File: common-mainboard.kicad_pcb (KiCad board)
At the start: 2 copper layers, 77.5 x 49.5 mm, 92 parts, among them J1 SIM_Card, J2 RSP-122811-01, J3 Conn_01x02_Female, J4 S4B-ZR-SM4A-TF(LF)(SN), Q1 DTC043ZEB, Q2 DTC043ZEB, Q3 DTC043ZEB, SW1 SW_Push, SW2 SW_Push, U1 ATSAMD21J18A-M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

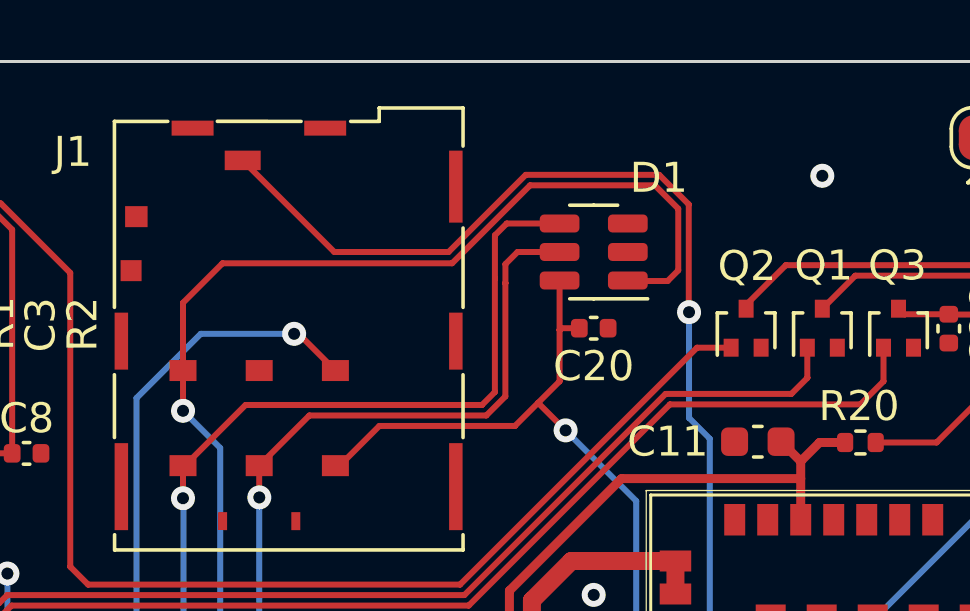
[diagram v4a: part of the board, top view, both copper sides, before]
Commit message: sim card: added RF filtering passive components
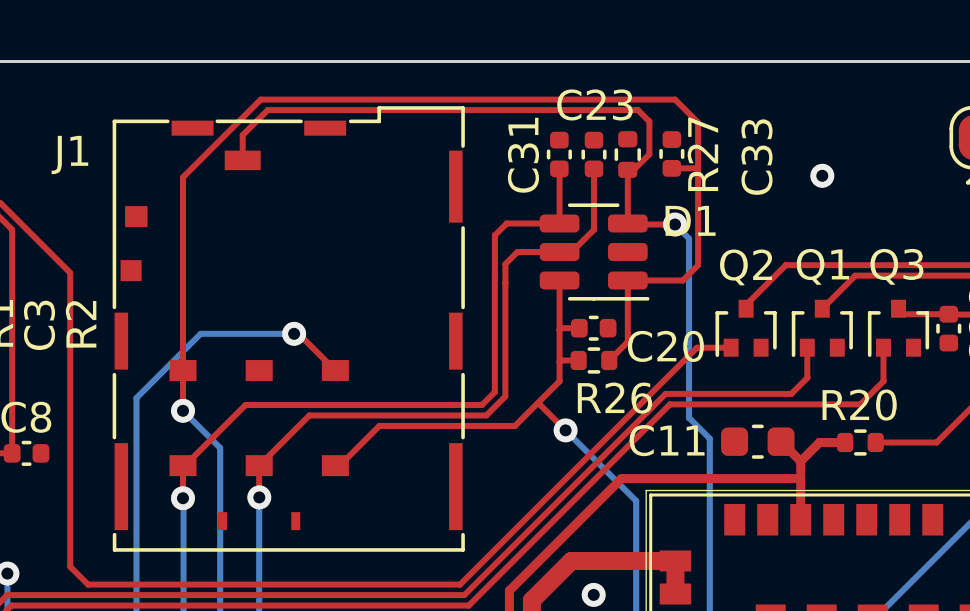
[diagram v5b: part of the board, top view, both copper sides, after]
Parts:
- added C23: 33pF, Capacitor_SMD:C_0402_1005Metric, F.Cu at (114.3, 104.7)
- added C31: 33pF, Capacitor_SMD:C_0402_1005Metric, F.Cu at (113.2, 104.7)
- added C33: 33pF, Capacitor_SMD:C_0402_1005Metric, F.Cu at (116.9, 104.7)
- added R26: 15k, Resistor_SMD:R_0402_1005Metric, F.Cu at (114.3, 111.6)
- added R27: 51k, Resistor_SMD:R_0402_1005Metric, F.Cu at (115.4, 104.7)
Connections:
- D1 pad 3: unconnected-(D1-Pad3) -> USIM1_DET
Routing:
- net USIM1_DATA: track 58.7 -> 70.2 mm
- net USIM1_RST: track 44.7 -> 48.2 mm
- net USIM1_DET: track 42.5 -> 44.7 mm
- net USIM1_CLK: track 50.7 -> 52.5 mm
- net USIM1_VDD: track 33.3 -> 34.0 mm

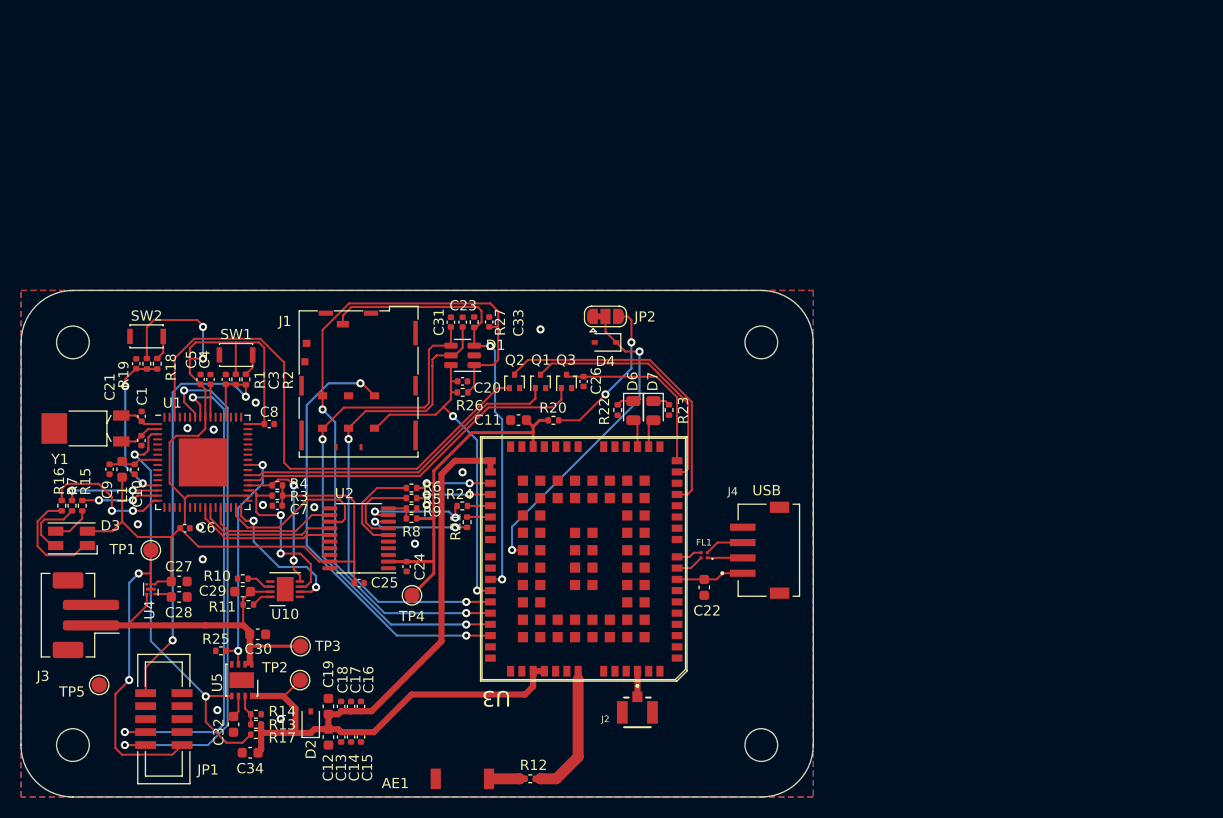
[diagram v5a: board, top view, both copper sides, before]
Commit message: added connectors for I2C and SPI extensions
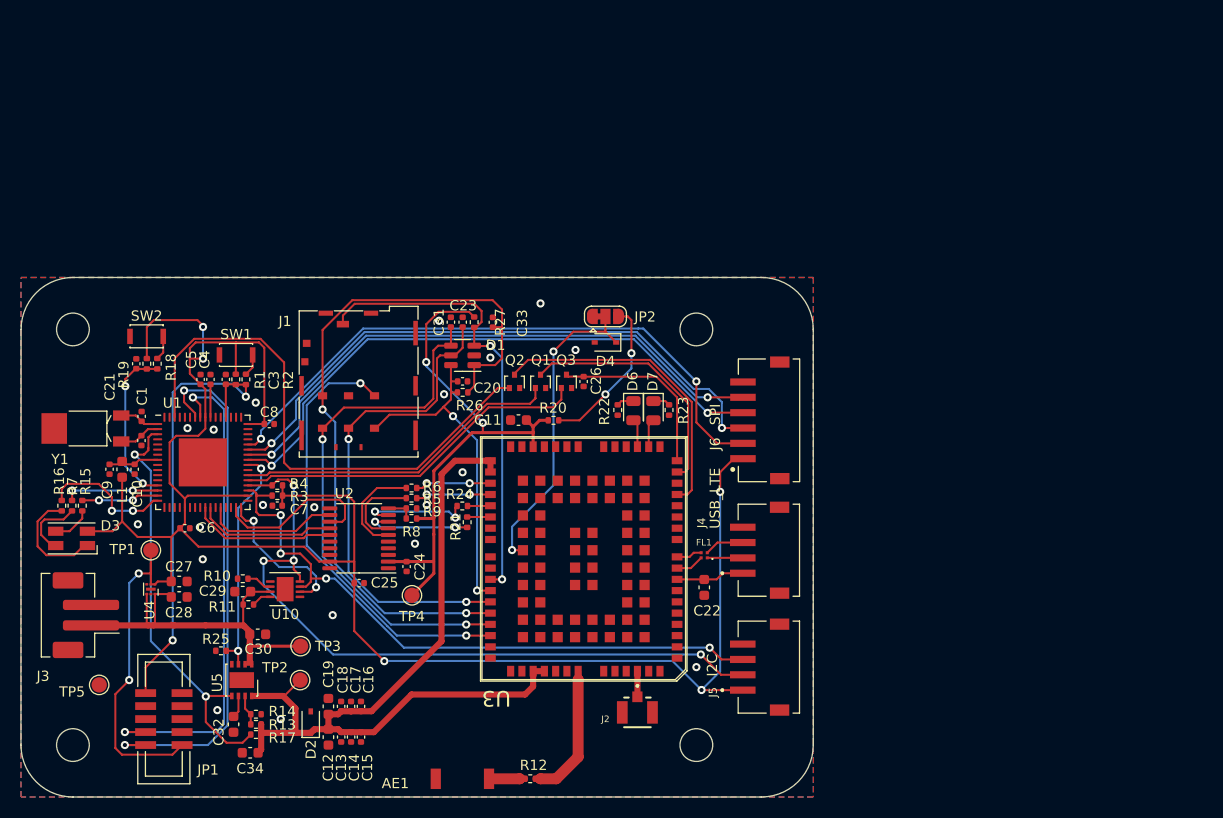
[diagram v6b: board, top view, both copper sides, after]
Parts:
- added J5: S4B-ZR-SM4A-TF(LF)(SN), S4B-ZR-SM4A-TF_LF__SN_:JST_S4B-ZR-SM4A-TF(LF)(SN), F.Cu at (141.7, 138.4)
- added J6: S6B-ZR-SM4A-TF(LF)(SN), S6B-ZR-SM4A-TF_LF__SN_:JST_S6B-ZR-SM4A-TF(LF)(SN), F.Cu at (141.7, 114.3)
- moved H3 6.48 mm to (137.2, 105.4)
- moved H2 6.35 mm to (137.2, 146.1)
- moved H4 1.27 mm to (76.2, 105.4)
- moved C33 0.36 mm to (117.3, 104.7)
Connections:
- U1 pad 41: unconnected-(U1-Pad41) -> MISO
- U1 pad 42: unconnected-(U1-Pad42) -> /CS
- U1 pad 43: unconnected-(U1-Pad43) -> MOSI
- U1 pad 44: unconnected-(U1-Pad44) -> SCK
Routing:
- net +3V3: track 150.0 -> 219.9 mm, vias 4 -> 7
- net SCK: track 0.00 -> 60.6 mm, vias 0 -> 2
- net MOSI: track 0.00 -> 59.6 mm, vias 0 -> 2
- net MISO: track 0.00 -> 58.5 mm, vias 0 -> 2
- net /CS: track 0.00 -> 57.1 mm, vias 0 -> 2
- net SCL: track 14.6 -> 70.4 mm, vias 2 -> 4
- net SDA: track 17.0 -> 62.5 mm, vias 2 -> 4
- net VDD_EXT: track 35.2 -> 53.5 mm, vias 0 -> 2
- net USIM1_DATA: track 70.2 -> 71.3 mm
- net VBAT: track 39.4 -> 38.7 mm
- net GNDREF: vias 14 -> 20
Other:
- board size 77.5 x 49.5 mm -> 77.5 x 50.8 mm
- board text added: "I2C"
- board text added: "SPI"
- board text added: "USB_LTE"
- board text removed: "USB"

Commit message: updated footprints and PCB
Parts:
- C32: footprint Capacitor_SMD:C_0603_1608Metric -> Capacitor_SMD:C_0201_0603Metric
- C34: value 1uF -> 10uF
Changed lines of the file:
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@@
     )
   )
-  (footprint "Capacitor_SMD:C_0603_1608Metric" (layer "F.Cu")
+  (footprint "Capacitor_SMD:C_0201_0603Metric" (layer "F.Cu")
     (at 91.904857 144.026066 -90)
-    (descr "Capacitor SMD 0603 (1608 Metric), square (rectangular) end terminal, IPC_7351 nominal, (Body size source: IPC-SM-782 page 76, https://www.pcb-3d.com/wordpress/wp-content/uploads/ipc-sm-782a_amendment_1_and_2.pdf), generated with kicad-footprint-generator")
+    (descr "Capacitor SMD 0201 (0603 Metric), square (rectangular) end terminal, IPC_7351 nominal, (Body size source: https://www.vishay.com/docs/20052/crcw0201e3.pdf), generated with kicad-footprint-generator")
     (tags "capacitor")
     (property "Sheetfile" "lipo-power-supply.kicad_sch")
     (property "Sheetname" "lipo-power-supply")
     (attr smd)
-    (fp_text reference "C32" (at 0.753934 1.443504 90) (layer "F.SilkS")
+    (fp_text reference "C32" (at 0 -1.05 -90) (layer "F.SilkS")
       (effects (font (size 1 1) (thickness 0.15)))
     )
-    (fp_text value "1000pF" (at 0 1.43 90) (layer "F.Fab")
+    (fp_text value "1000pF" (at 0 1.05 -90) (layer "F.Fab")
       (effects (font (size 1 1) (thickness 0.15)))
     )
-    (fp_text user "${REFERENCE}" (at 0 0 90) (layer "F.Fab")
-      (effects (font (size 0.4 0.4) (thickness 0.06)))
+    (fp_text user "${REFERENCE}" (at 0 -0.68 -90) (layer "F.Fab")
+      (effects (font (size 0.25 0.25) (thickness 0.04)))
     )
-    (fp_line (start -0.14058 -0.51) (end 0.14058 -0.51) (layer "F.SilkS") (width 0.12))
-    (fp_line (start -0.14058 0.51) (end 0.14058 0.51) (layer "F.SilkS") (width 0.12))
-    (fp_line (start 1.48 0.73) (end -1.48 0.73) (layer "F.CrtYd") (width 0.05))
-    (fp_line (start 1.48 -0.73) (end 1.48 0.73) (layer "F.CrtYd") (width 0.05))
-    (fp_line (start -1.48 0.73) (end -1.48 -0.73) (layer "F.CrtYd") (width 0.05))
-    (fp_line (start -1.48 -0.73) (end 1.48 -0.73) (layer "F.CrtYd") (width 0.05))
-    (fp_line (start -0.8 -0.4) (end 0.8 -0.4) (layer "F.Fab") (width 0.1))
-    (fp_line (start -0.8 0.4) (end -0.8 -0.4) (layer "F.Fab") (width 0.1))
-    (fp_line (start 0.8 0.4) (end -0.8 0.4) (layer "F.Fab") (width 0.1))
-    (fp_line (start 0.8 -0.4) (end 0.8 0.4) (layer "F.Fab") (width 0.1))
-    (pad "1" smd roundrect (at -0.775 0 270) (size 0.9 0.95) (layers "F.Cu" "F.Paste" "F.Mask") (roundrect_rratio 0.25)
+    (fp_line (start 0.7 0.35) (end -0.7 0.35) (layer "F.CrtYd") (width 0.05))
+    (fp_line (start 0.7 -0.35) (end 0.7 0.35) (layer "F.CrtYd") (width 0.05))
+    (fp_line (start -0.7 0.35) (end -0.7 -0.35) (layer "F.CrtYd") (width 0.05))
+    (fp_line (start -0.7 -0.35) (end 0.7 -0.35) (layer "F.CrtYd") (width 0.05))
+    (fp_line (start -0.3 -0.15) (end 0.3 -0.15) (layer "F.Fab") (width 0.1))
+    (fp_line (start -0.3 0.15) (end -0.3 -0.15) (layer "F.Fab") (width 0.1))
+    (fp_line (start 0.3 0.15) (end -0.3 0.15) (layer "F.Fab") (width 0.1))
+    (fp_line (start 0.3 -0.15) (end 0.3 0.15) (layer "F.Fab") (width 0.1))
+    (pad "" smd roundrect (at 0.345 0 270) (size 0.318 0.36) (layers "F.Paste") (roundrect_rratio 0.25))
+    (pad "" smd roundrect (at -0.345 0 270) (size 0.318 0.36) (layers "F.Paste") (roundrect_rratio 0.25))
+    (pad "1" smd roundrect (at -0.32 0 270) (size 0.46 0.4) (layers "F.Cu" "F.Mask") (roundrect_rratio 0.25)
       (net 53 "Net-(C32-Pad1)") (pintype "passive"))
-    (pad "2" smd roundrect (at 0.775 0 270) (size 0.9 0.95) (layers "F.Cu" "F.Paste" "F.Mask") (roundrect_rratio 0.25)
+    (pad "2" smd roundrect (at 0.32 0 270) (size 0.46 0.4) (layers "F.Cu" "F.Mask") (roundrect_rratio 0.25)
       (net 2 "GNDREF") (pintype "passive"))
-    (model "${KICAD6_3DMODEL_DIR}/Capacitor_SMD.3dshapes/C_0603_1608Metric.wrl"
+    (model "${KICAD6_3DMODEL_DIR}/Capacitor_SMD.3dshapes/C_0201_0603Metric.wrl"
       (offset (xyz 0 0 0))
       (scale (xyz 1 1 1))
@@
       (effects (font (size 1 1) (thickness 0.15)))
     )
-    (fp_text value "1uF" (at 0 1.43) (layer "F.Fab")
+    (fp_text value "10uF" (at 0 1.43) (layer "F.Fab")
       (effects (font (size 1 1) (thickness 0.15)))
     )
@@
   (segment (start 92.385 141.25) (end 92.385 142.770923) (width 0.2) (layer "F.Cu") (net 53))
   (segment (start 92.385 142.770923) (end 91.904857 143.251066) (width 0.2) (layer "F.Cu") (net 53))
+  (segment (start 91.904857 143.251066) (end 91.904857 143.706066) (width 0.2) (layer "F.Cu") (net 53))
   (segment (start 84.4875 115.16) (end 83.538085 115.16) (width 0.2) (layer "F.Cu") (net 54))
   (segment (start 80.923405 116.366368) (end 82.331717 116.366368) (width 0.2) (layer "F.Cu") (net 54))

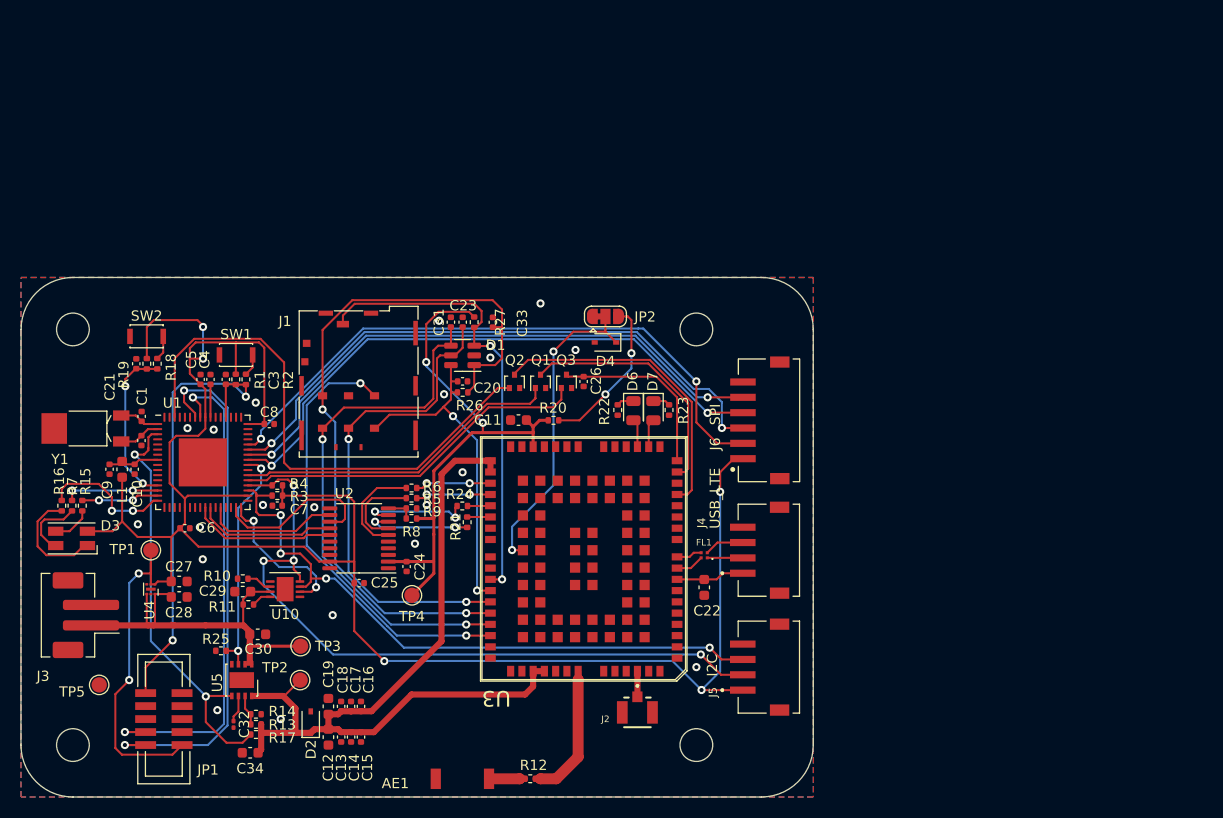
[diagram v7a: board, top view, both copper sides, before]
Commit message: fixed SIM card orientation
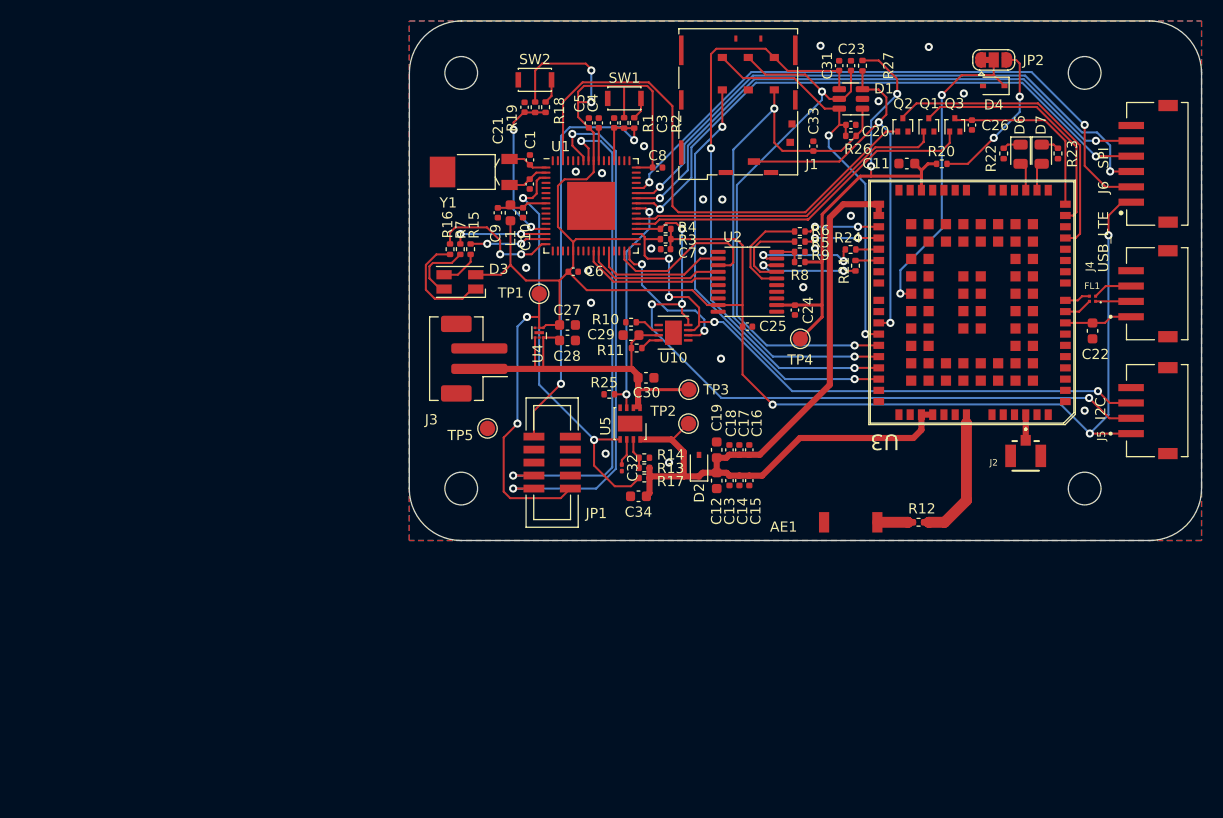
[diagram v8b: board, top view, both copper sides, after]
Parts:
- added G***: LOGO, LOGO, B.Cu at (147.2, 100.7)
- moved J1 50.1 mm to (142.2, 81.3), turned to 0 degrees
- moved R23 45.6 mm to (172.5, 88.2)
- moved AE1 45.5 mm to (151.9, 129.3)
- moved C12 45.5 mm to (139.1, 120.2)
- moved C13 45.5 mm to (140.4, 120.2)
- moved C20 45.5 mm to (152.3, 85.4)
- moved C23 45.5 mm to (152.3, 79.6)
- moved C3 45.5 mm to (129.1, 85.2)
- moved C34 45.5 mm to (131.5, 121.7)
- moved C7 45.5 mm to (134.2, 97.6)
- moved D1 45.5 mm to (152.3, 82.9)
- moved Q3 45.5 mm to (162.4, 85.4)
- moved TP4 45.5 mm to (147.3, 106.3)
- moved C15 45.5 mm to (142.3, 120.2)
- moved C16 45.5 mm to (139.1, 117.2)
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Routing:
- net USIM1_DATA: track 71.3 -> 54.9 mm
- net USIM1_VDD: track 34.0 -> 40.5 mm
- net USIM1_CLK: track 52.2 -> 58.7 mm
- net USIM1_RST: track 48.0 -> 54.5 mm
- net VDD_EXT: track 53.5 -> 49.8 mm
- net USIM1_DET: track 45.0 -> 42.2 mm
- net +3V3: track 219.9 -> 217.8 mm
- net USIM1_GND: track 43.4 -> 42.2 mm
- net GNDREF: vias 20 -> 21
